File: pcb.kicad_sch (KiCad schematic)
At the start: 21 parts

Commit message: Footprint assignment
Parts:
- MX1, MX10, MX2, MX3, MX4, MX5, MX6, MX7, MX8, MX9: renamed from MX?; footprint (none) -> Button_Switch_Keyboard:SW_Cherry_MX_1.00u_PCB
- U1: renamed from U?; footprint RPi_Pico:RPi_Pico_SMD_TH -> MCU_RaspberryPi_and_Boards:RPi_Pico_SMD_TH
- gave numbers to parts that had none: 10

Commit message: Initial PCB layout
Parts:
- MX1, MX10, MX2, MX3, MX4, MX5, MX6, MX7, MX8, MX9: footprint Button_Switch_Keyboard:SW_Cherry_MX_1.00u_PCB -> MX_Only:MXOnly-1U
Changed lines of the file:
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@@
       (effects (font (size 0.508 0.508)))
     )
-    (property "Footprint" "Button_Switch_Keyboard:SW_Cherry_MX_1.00u_PCB" (id 2) (at 187.325 89.535 0)
+    (property "Footprint" "MX_Only:MXOnly-1U" (id 2) (at 187.325 89.535 0)
       (effects (font (size 1.524 1.524)) hide)
     )
@@
       (effects (font (size 0.508 0.508)))
     )
-    (property "Footprint" "Button_Switch_Keyboard:SW_Cherry_MX_1.00u_PCB" (id 2) (at 211.455 79.375 0)
+    (property "Footprint" "MX_Only:MXOnly-1U" (id 2) (at 211.455 79.375 0)
       (effects (font (size 1.524 1.524)) hide)
     )
@@
       (effects (font (size 0.508 0.508)))
     )
-    (property "Footprint" "Button_Switch_Keyboard:SW_Cherry_MX_1.00u_PCB" (id 2) (at 231.775 79.375 0)
+    (property "Footprint" "MX_Only:MXOnly-1U" (id 2) (at 231.775 79.375 0)
       (effects (font (size 1.524 1.524)) hide)
     )
@@
       (effects (font (size 0.508 0.508)))
     )
-    (property "Footprint" "Button_Switch_Keyboard:SW_Cherry_MX_1.00u_PCB" (id 2) (at 197.485 99.695 0)
+    (property "Footprint" "MX_Only:MXOnly-1U" (id 2) (at 197.485 99.695 0)
       (effects (font (size 1.524 1.524)) hide)
     )
@@
       (effects (font (size 0.508 0.508)))
     )
-    (property "Footprint" "Button_Switch_Keyboard:SW_Cherry_MX_1.00u_PCB" (id 2) (at 177.165 79.375 0)
+    (property "Footprint" "MX_Only:MXOnly-1U" (id 2) (at 177.165 79.375 0)
       (effects (font (size 1.524 1.524)) hide)
     )
@@
       (effects (font (size 0.508 0.508)))
     )
-    (property "Footprint" "Button_Switch_Keyboard:SW_Cherry_MX_1.00u_PCB" (id 2) (at 197.485 79.375 0)
+    (property "Footprint" "MX_Only:MXOnly-1U" (id 2) (at 197.485 79.375 0)
       (effects (font (size 1.524 1.524)) hide)
     )
@@
       (effects (font (size 0.508 0.508)))
     )
-    (property "Footprint" "Button_Switch_Keyboard:SW_Cherry_MX_1.00u_PCB" (id 2) (at 211.455 99.695 0)
+    (property "Footprint" "MX_Only:MXOnly-1U" (id 2) (at 211.455 99.695 0)
       (effects (font (size 1.524 1.524)) hide)
     )
@@
       (effects (font (size 0.508 0.508)))
     )
-    (property "Footprint" "Button_Switch_Keyboard:SW_Cherry_MX_1.00u_PCB" (id 2) (at 177.165 99.695 0)
+    (property "Footprint" "MX_Only:MXOnly-1U" (id 2) (at 177.165 99.695 0)
       (effects (font (size 1.524 1.524)) hide)
     )
@@
       (effects (font (size 0.508 0.508)))
     )
-    (property "Footprint" "Button_Switch_Keyboard:SW_Cherry_MX_1.00u_PCB" (id 2) (at 231.775 99.695 0)
+    (property "Footprint" "MX_Only:MXOnly-1U" (id 2) (at 231.775 99.695 0)
       (effects (font (size 1.524 1.524)) hide)
     )
@@
       (effects (font (size 0.508 0.508)))
     )
-    (property "Footprint" "Button_Switch_Keyboard:SW_Cherry_MX_1.00u_PCB" (id 2) (at 221.615 89.535 0)
+    (property "Footprint" "MX_Only:MXOnly-1U" (id 2) (at 221.615 89.535 0)
       (effects (font (size 1.524 1.524)) hide)
     )
@@
     )
     (path "/766fdfb3-db19-48c2-b779-b910c8a2ecfb"
-      (reference "MX1") (unit 1) (value "MX-LED") (footprint "Button_Switch_Keyboard:SW_Cherry_MX_1.00u_PCB")
+      (reference "MX1") (unit 1) (value "MX-LED") (footprint "MX_Only:MXOnly-1U")
     )
     (path "/9b58b2b3-67cf-495f-b667-1ffb1ad1d5b8"
-      (reference "MX2") (unit 1) (value "MX-LED") (footprint "Button_Switch_Keyboard:SW_Cherry_MX_1.00u_PCB")
+      (reference "MX2") (unit 1) (value "MX-LED") (footprint "MX_Only:MXOnly-1U")
     )
     (path "/0a212509-b99d-4c27-a7b8-116754ebdf67"
-      (reference "MX3") (unit 1) (value "MX-LED") (footprint "Button_Switch_Keyboard:SW_Cherry_MX_1.00u_PCB")
+      (reference "MX3") (unit 1) (value "MX-LED") (footprint "MX_Only:MXOnly-1U")
     )
     (path "/78e64fc1-c1e1-4345-a497-d1b849807ee4"
-      (reference "MX4") (unit 1) (value "MX-LED") (footprint "Button_Switch_Keyboard:SW_Cherry_MX_1.00u_PCB")
+      (reference "MX4") (unit 1) (value "MX-LED") (footprint "MX_Only:MXOnly-1U")
     )
     (path "/536a524e-0516-416a-9f6f-926f774c2cf8"
-      (reference "MX5") (unit 1) (value "MX-LED") (footprint "Button_Switch_Keyboard:SW_Cherry_MX_1.00u_PCB")
+      (reference "MX5") (unit 1) (value "MX-LED") (footprint "MX_Only:MXOnly-1U")
     )
     (path "/1e1d7dc6-b41a-409a-bf45-fae7b6730171"
-      (reference "MX6") (unit 1) (value "MX-LED") (footprint "Button_Switch_Keyboard:SW_Cherry_MX_1.00u_PCB")
+      (reference "MX6") (unit 1) (value "MX-LED") (footprint "MX_Only:MXOnly-1U")
     )
     (path "/8a292752-b364-49e7-86b0-b59a11d1e51a"
-      (reference "MX7") (unit 1) (value "MX-LED") (footprint "Button_Switch_Keyboard:SW_Cherry_MX_1.00u_PCB")
+      (reference "MX7") (unit 1) (value "MX-LED") (footprint "MX_Only:MXOnly-1U")
     )
     (path "/f03166d2-869e-43f3-9697-a4505fe31560"
-      (reference "MX8") (unit 1) (value "MX-LED") (footprint "Button_Switch_Keyboard:SW_Cherry_MX_1.00u_PCB")
+      (reference "MX8") (unit 1) (value "MX-LED") (footprint "MX_Only:MXOnly-1U")
     )
     (path "/46f77868-e63b-46ae-b810-eeaefd31eed7"
-      (reference "MX9") (unit 1) (value "MX-LED") (footprint "Button_Switch_Keyboard:SW_Cherry_MX_1.00u_PCB")
+      (reference "MX9") (unit 1) (value "MX-LED") (footprint "MX_Only:MXOnly-1U")
     )
     (path "/cda60508-e18b-4fc3-b5b3-8870ee6e8fe9"
-      (reference "MX10") (unit 1) (value "MX-LED") (footprint "Button_Switch_Keyboard:SW_Cherry_MX_1.00u_PCB")
+      (reference "MX10") (unit 1) (value "MX-LED") (footprint "MX_Only:MXOnly-1U")
     )
     (path "/430d1463-de71-4131-a362-3f573ce8f2df"

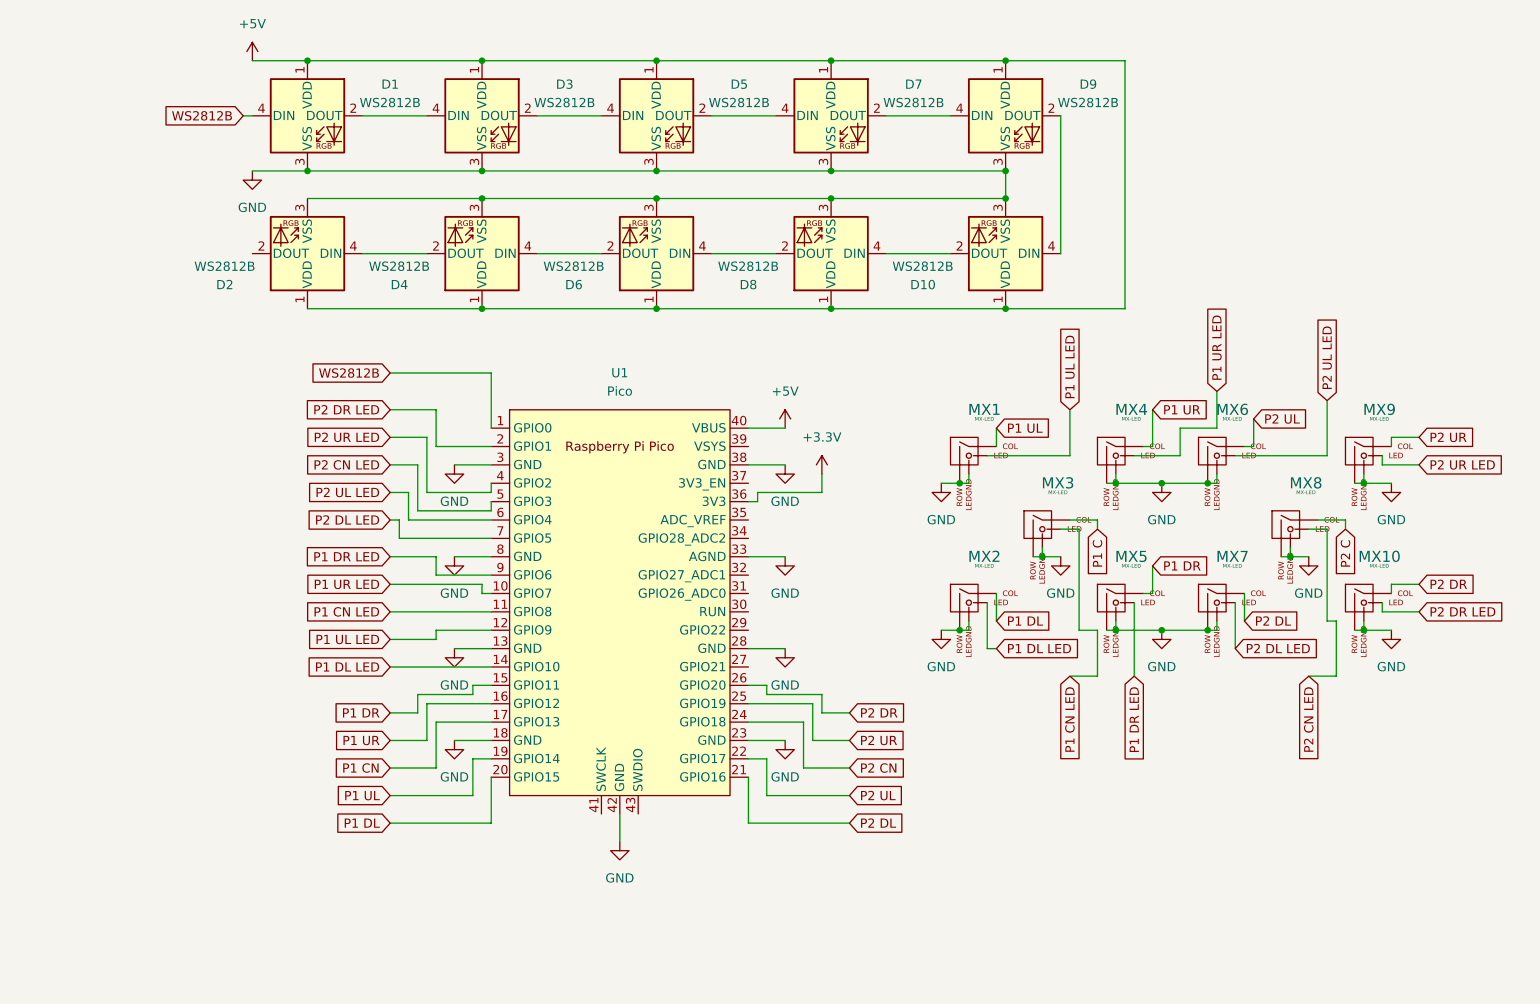
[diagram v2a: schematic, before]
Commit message: P2 initial routing done
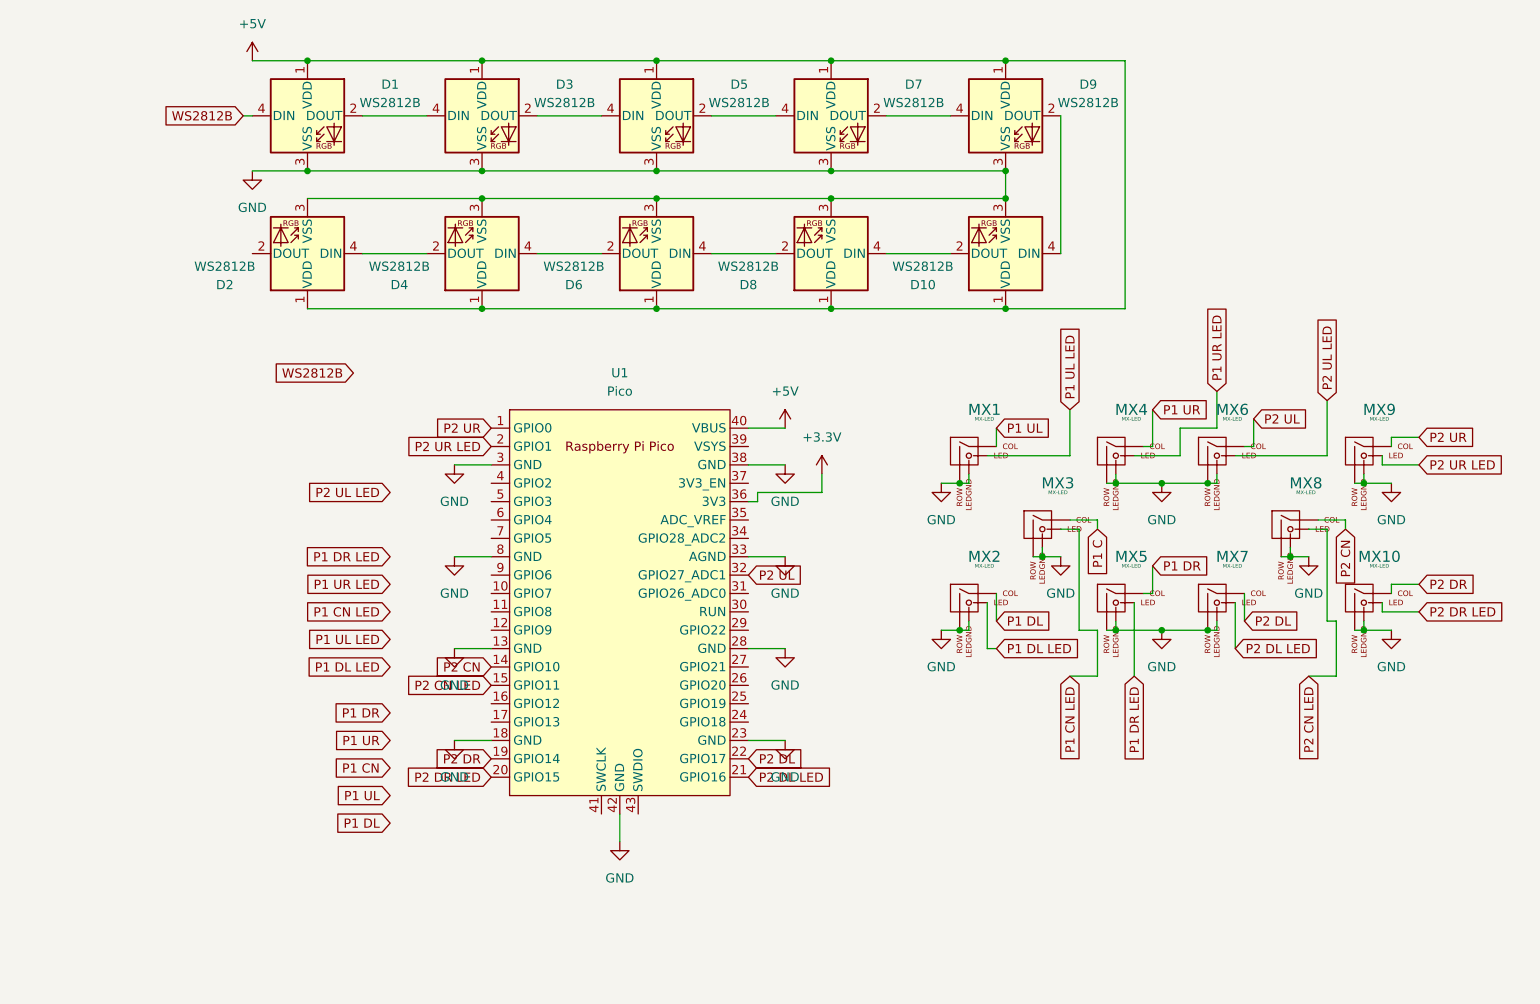
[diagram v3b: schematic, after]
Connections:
- net P2 C is gone; now on net P2 CN: MX8.1 (COL)
- net P1 CN: no longer U1.17 (GPIO13)
- net P1 CN LED: no longer U1.11 (GPIO8)
- net P1 DL: no longer U1.20 (GPIO15)
- net P1 DL LED: no longer U1.14 (GPIO10)
- net P1 DR: no longer U1.15 (GPIO11)
- net P1 DR LED: no longer U1.9 (GPIO6)
- net P1 UL: no longer U1.19 (GPIO14)
- net P1 UL LED: no longer U1.12 (GPIO9)
- net P1 UR: no longer U1.16 (GPIO12)
- net P1 UR LED: no longer U1.10 (GPIO7)
- net P2 CN: now also U1.14 (GPIO10); no longer U1.24 (GPIO18)
- net P2 CN LED: now also U1.15 (GPIO11); no longer U1.5 (GPIO3)
- net P2 DL: now also U1.22 (GPIO17); no longer U1.21 (GPIO16)
- net P2 DL LED: now also U1.21 (GPIO16); no longer U1.7 (GPIO5)
- net P2 DR: now also U1.19 (GPIO14); no longer U1.26 (GPIO20)
- net P2 DR LED: now also U1.20 (GPIO15); no longer U1.2 (GPIO1)
- net P2 UL: now also U1.32 (GPIO27_ADC1); no longer U1.22 (GPIO17)
- net P2 UL LED: no longer U1.6 (GPIO4)
- net P2 UR: now also U1.1 (GPIO0); no longer U1.25 (GPIO19)
- net P2 UR LED: now also U1.2 (GPIO1); no longer U1.4 (GPIO2)
- net WS2812B: no longer U1.1 (GPIO0)

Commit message: P1 initial routing, no more WS2812Bs built in
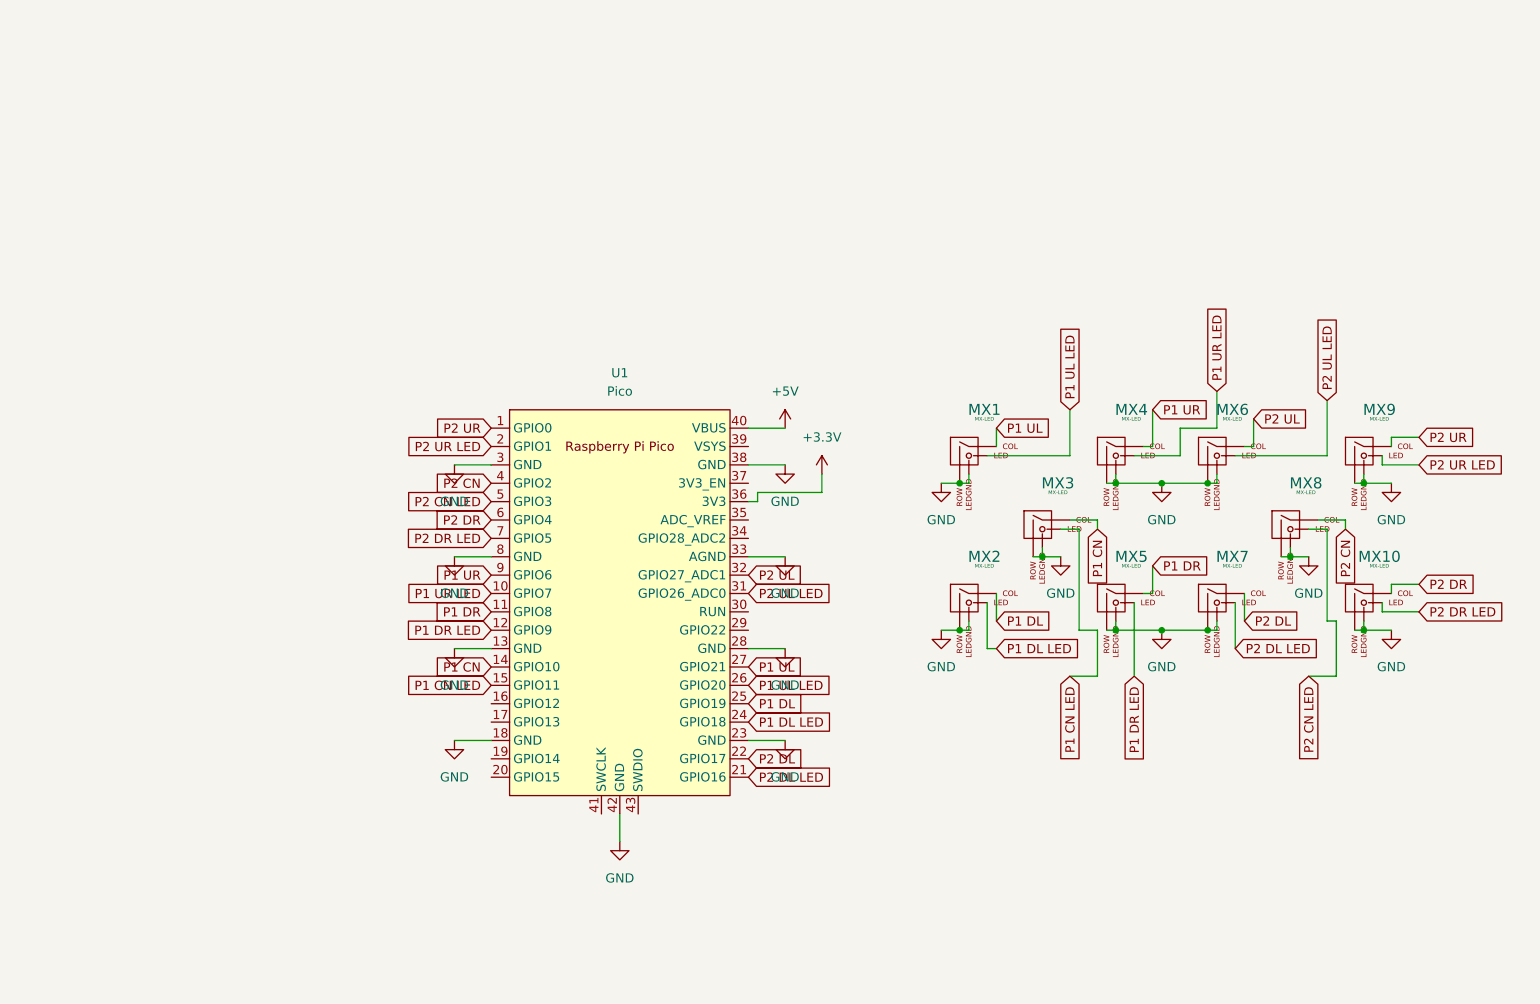
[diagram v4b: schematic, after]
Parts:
- removed D1, D10, D2, D3, D4, D5, D6, D7, D8, D9: WS2812B, LED_SMD:LED_WS2812B_PLCC4_5.0x5.0mm_P3.2mm, symbol LED:WS2812B
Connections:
- net P1 C is gone; now on net P1 CN: MX3.1 (COL)
- net P1 CN: now also U1.14 (GPIO10)
- net P1 CN LED: now also U1.15 (GPIO11)
- net P1 DL: now also U1.25 (GPIO19)
- net P1 DL LED: now also U1.24 (GPIO18)
- net P1 DR: now also U1.11 (GPIO8)
- net P1 DR LED: now also U1.12 (GPIO9)
- net P1 UL: now also U1.27 (GPIO21)
- net P1 UL LED: now also U1.26 (GPIO20)
- net P1 UR: now also U1.9 (GPIO6)
- net P1 UR LED: now also U1.10 (GPIO7)
- net P2 CN: now also U1.4 (GPIO2); no longer U1.14 (GPIO10)
- net P2 CN LED: now also U1.5 (GPIO3); no longer U1.15 (GPIO11)
- net P2 DR: now also U1.6 (GPIO4); no longer U1.19 (GPIO14)
- net P2 DR LED: now also U1.7 (GPIO5); no longer U1.20 (GPIO15)
- net P2 UL LED: now also U1.31 (GPIO26_ADC0)

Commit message: ooooo fancy pcb art (+ silkscreen adjustments)
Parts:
- added D1, D10, D2, D3, D4, D5, D6, D7, D8, D9: WS2812B, LED_SMD:LED_WS2812B_PLCC4_5.0x5.0mm_P3.2mm, symbol LED:WS2812B
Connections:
- net +5V: now also D1.1 (VDD), D10.1 (VDD), D2.1 (VDD), D3.1 (VDD), D4.1 (VDD), D5.1 (VDD), D6.1 (VDD), D7.1 (VDD), D8.1 (VDD), D9.1 (VDD)
- net GND: now also D1.3 (VSS), D10.3 (VSS), D2.3 (VSS), D3.3 (VSS), D4.3 (VSS), D5.3 (VSS), D6.3 (VSS), D7.3 (VSS), D8.3 (VSS), D9.3 (VSS)
- net DIN: now reaches U1.29 (GPIO22)
- net DIN: now also D1.4 (DIN)
- new net: D5.2 (DOUT), D7.4 (DIN)
- new net: D3.2 (DOUT), D5.4 (DIN)
- new net: D7.2 (DOUT), D9.4 (DIN)
- new net: D1.2 (DOUT), D3.4 (DIN)
- new net: D10.2 (DOUT), D8.4 (DIN)
- new net: D10.4 (DIN), D9.2 (DOUT)
- new net: D4.4 (DIN), D6.2 (DOUT)
- new net: D6.4 (DIN), D8.2 (DOUT)
- new net: D2.4 (DIN), D4.2 (DOUT)

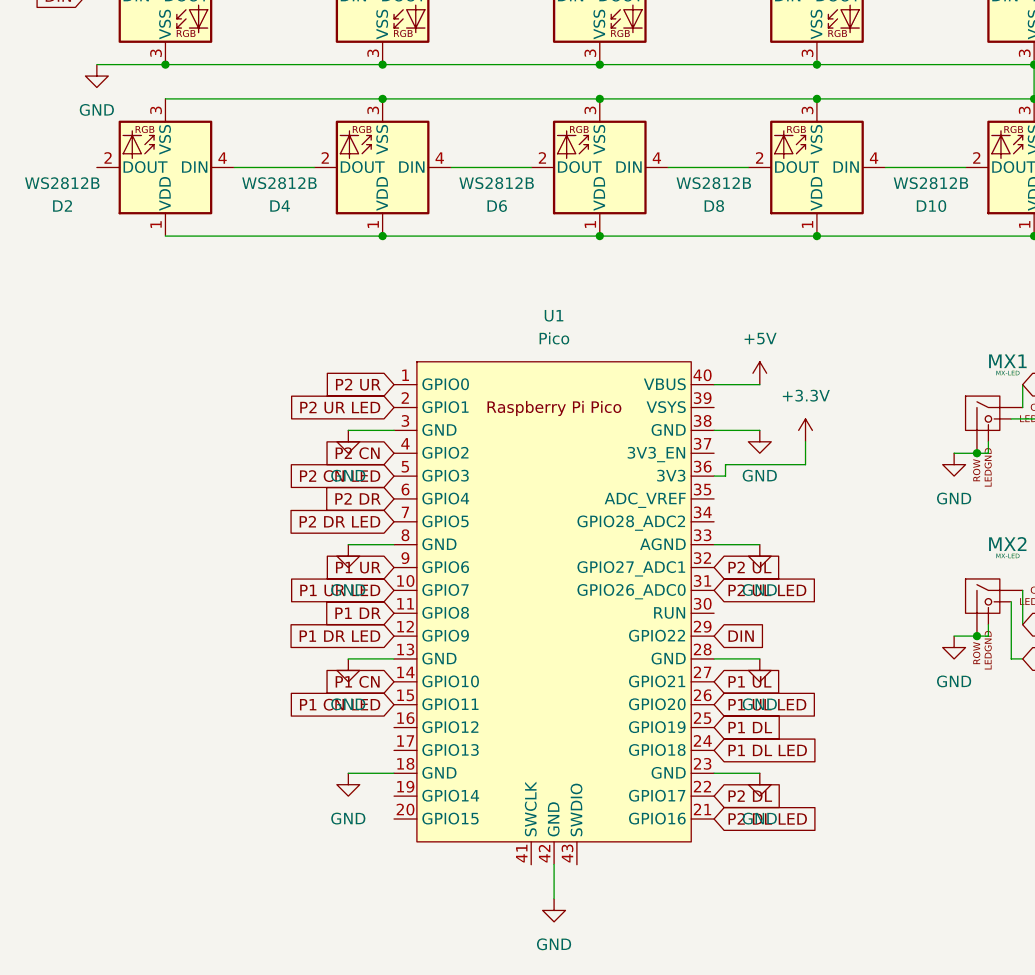
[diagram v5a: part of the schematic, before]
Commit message: Clean up schematic, PCB adjustments
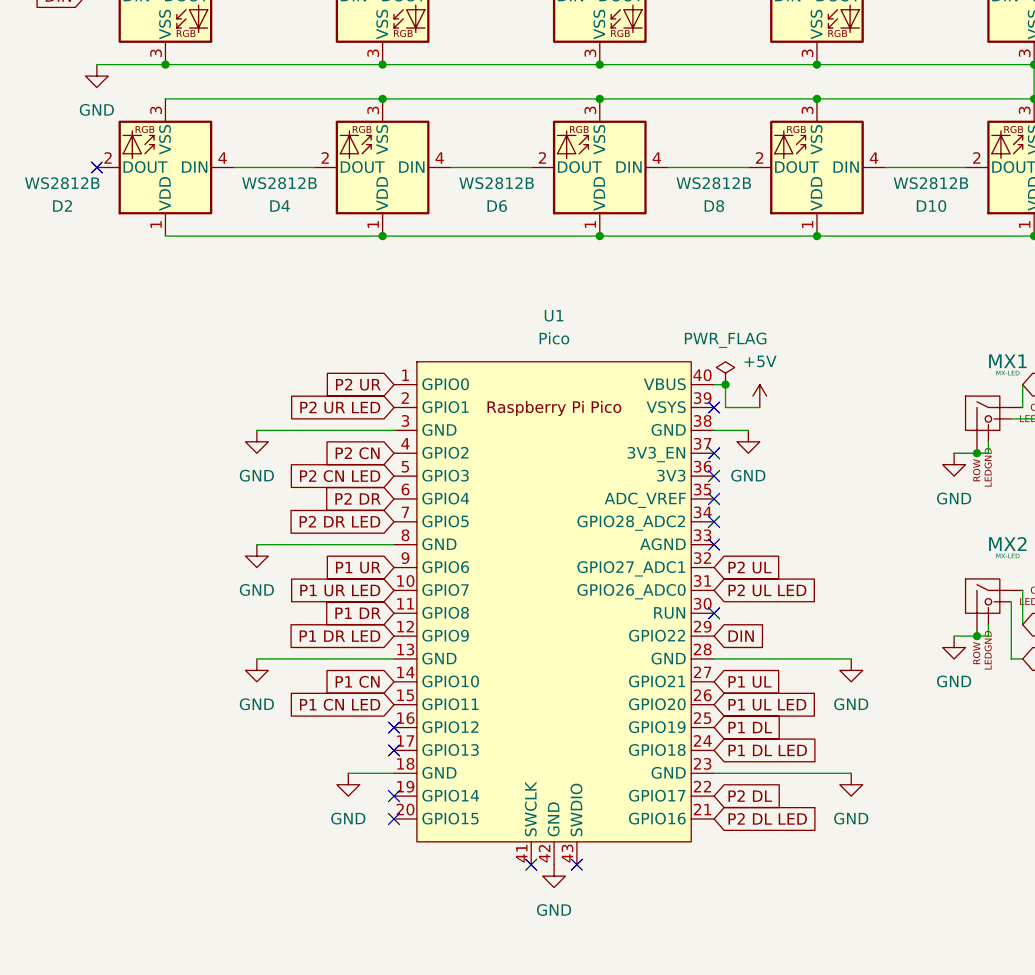
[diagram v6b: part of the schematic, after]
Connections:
- net GND: no longer U1.33 (AGND)
- net +3.3V: no longer names the net of U1.36 (3V3)
- no-connect marks 0 -> 14
